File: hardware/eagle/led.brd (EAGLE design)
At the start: 160 x 100 mm, 15 parts, among them IC1 MCP1406SOIC8, IC10 MCP1406SOIC8, IC11 MCP1406SOIC8, IC12 MCP1406SOIC8, IC13 MCP2551SOIC8, IC2 MCP1406SOIC8, IC3 MCP1406SOIC8, IC4 MCP1406SOIC8, IC5 MCP1406SOIC8, IC6 MCP1406SOIC8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

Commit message: neue boaerd version + datasheets added
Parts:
- removed JP1, JP2: (no value), pinhead:2X13
- added C2: (no value), rcl:E5-10,5
- added EXT1, EXT2: (no value), pinhead:2X13
- added IC14: 7805T, linear:TO220H
- added U$1, U$10, U$11, U$2, U$3, U$5, U$6, U$7, U$8, U$9: 2KLEMME, custom-parts:W237-102
- moved IC12 212.0 mm to (97.8, 74.9), flipped to the bottom
- moved IC10 189.5 mm to (82.5, 74.9), flipped to the bottom
- moved IC11 188.6 mm to (90.2, 74.9), flipped to the bottom
- moved IC13 167.5 mm to (50.8, 49.5), flipped to the bottom
- moved IC9 148.1 mm to (38.1, 74.9), flipped to the bottom
- moved IC6 144.5 mm to (90.2, 25.4), flipped to the bottom, turned to 180 degrees
- moved IC5 143.2 mm to (97.8, 25.4), flipped to the bottom, turned to 180 degrees
- moved IC4 142.0 mm to (105.4, 25.4), flipped to the bottom, turned to 180 degrees
- moved IC7 140.2 mm to (45.7, 74.9), flipped to the bottom
- moved IC8 139.3 mm to (53.3, 74.9), flipped to the bottom
- moved IC3 85.8 mm to (54.6, 25.4), flipped to the bottom, turned to 180 degrees
- moved IC2 84.6 mm to (62.2, 25.4), flipped to the bottom, turned to 180 degrees
- moved IC1 78.0 mm to (69.8, 25.4), flipped to the bottom, turned to 180 degrees
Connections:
- new net B1: EXT1.17, IC1.2
- new net B2: EXT1.26, IC4.2
- new net B3: EXT1.16, IC7.2
- new net B4: EXT2.10, IC10.2
- new net CANH: IC13.7, U$3.1
- new net CANL: IC13.6, U$3.2
- new net CANRX: EXT1.1, IC13.4
- new net CANTX: EXT1.3, IC13.1
- new net G1: EXT1.15, IC2.2
- new net G2: EXT1.22, IC5.2
- new net G3: EXT2.7, IC8.2
- new net G4: EXT2.8, IC11.2
- new net N$10: IC8.6, IC8.7, U$8.2
- new net N$11: IC7.6, IC7.7, U$7.1
- new net N$12: IC12.6, IC12.7, U$9.1
- new net N$13: IC11.6, IC11.7, U$9.2
- new net N$14: IC10.6, IC10.7, U$2.1
- new net N$2: C2.-, IC14.2, U$1.2
- new net N$3: IC3.6, IC3.7, U$5.1
- new net N$4: IC2.6, IC2.7, U$5.2
- new net N$5: IC1.6, IC1.7, U$6.1
- new net N$6: IC6.6, IC6.7, U$10.1
- new net N$7: IC5.6, IC5.7, U$10.2
- new net N$8: IC4.6, IC4.7, U$11.1
- new net N$9: IC9.6, IC9.7, U$8.1
- new net R1: EXT1.13, IC3.2
- new net R2: EXT1.21, IC6.2
- new net R3: EXT1.14, IC9.2
- new net R4: EXT2.4, IC12.2
- new net VCC: EXT2.26, IC13.3, IC14.3
- net +12V: now also C2.+, IC14.1, U$1.1, U$2.2
- net GND: now also EXT2.25, IC13.2, U$11.2, U$6.2, U$7.2
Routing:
- net R3: track 0.00 -> 45.8 mm
- net B3: track 0.00 -> 41.5 mm
- net B2: track 0.00 -> 33.5 mm
- net G2: track 0.00 -> 29.5 mm
- net R4: track 0.00 -> 28.7 mm
- net G4: track 0.00 -> 26.9 mm
- net G3: track 0.00 -> 26.5 mm
- net B4: track 0.00 -> 22.6 mm
- net R2: track 0.00 -> 21.6 mm
- net R1: track 0.00 -> 18.5 mm
- net G1: track 0.00 -> 14.9 mm
- net B1: track 0.00 -> 12.8 mm
- net CANRX: track 0.00 -> 11.3 mm
- net CANTX: track 0.00 -> 7.75 mm

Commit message: hardware changed
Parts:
- moved U$3 96.0 mm to (39.4, 3.81), turned to 0 degrees
- moved IC9 24.1 mm to (62.2, 74.9)
- moved IC13 16.3 mm to (40.6, 36.8), turned to 270 degrees
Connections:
- net +12V: no longer U$2.2
- net B3: now also EXT1.14; no longer EXT1.16
- net G3: now also EXT1.16; no longer EXT2.7
- net GND: now also U$2.2
- net R3: now also EXT2.7; no longer EXT1.14
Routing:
- net +12V: track 0.00 -> 119.6 mm
- net CANH: track 0.00 -> 41.1 mm
- net CANL: track 0.00 -> 34.9 mm
- net R3: track 45.8 -> 21.8 mm
- net N$8: track 0.00 -> 20.7 mm
- net N$11: track 0.00 -> 19.2 mm
- net CANRX: track 11.3 -> 0.00 mm
- net CANTX: track 7.75 -> 17.3 mm
- net B3: track 41.5 -> 34.4 mm
- net G3: track 26.5 -> 32.0 mm
- added copper zone on layer 16, net GND

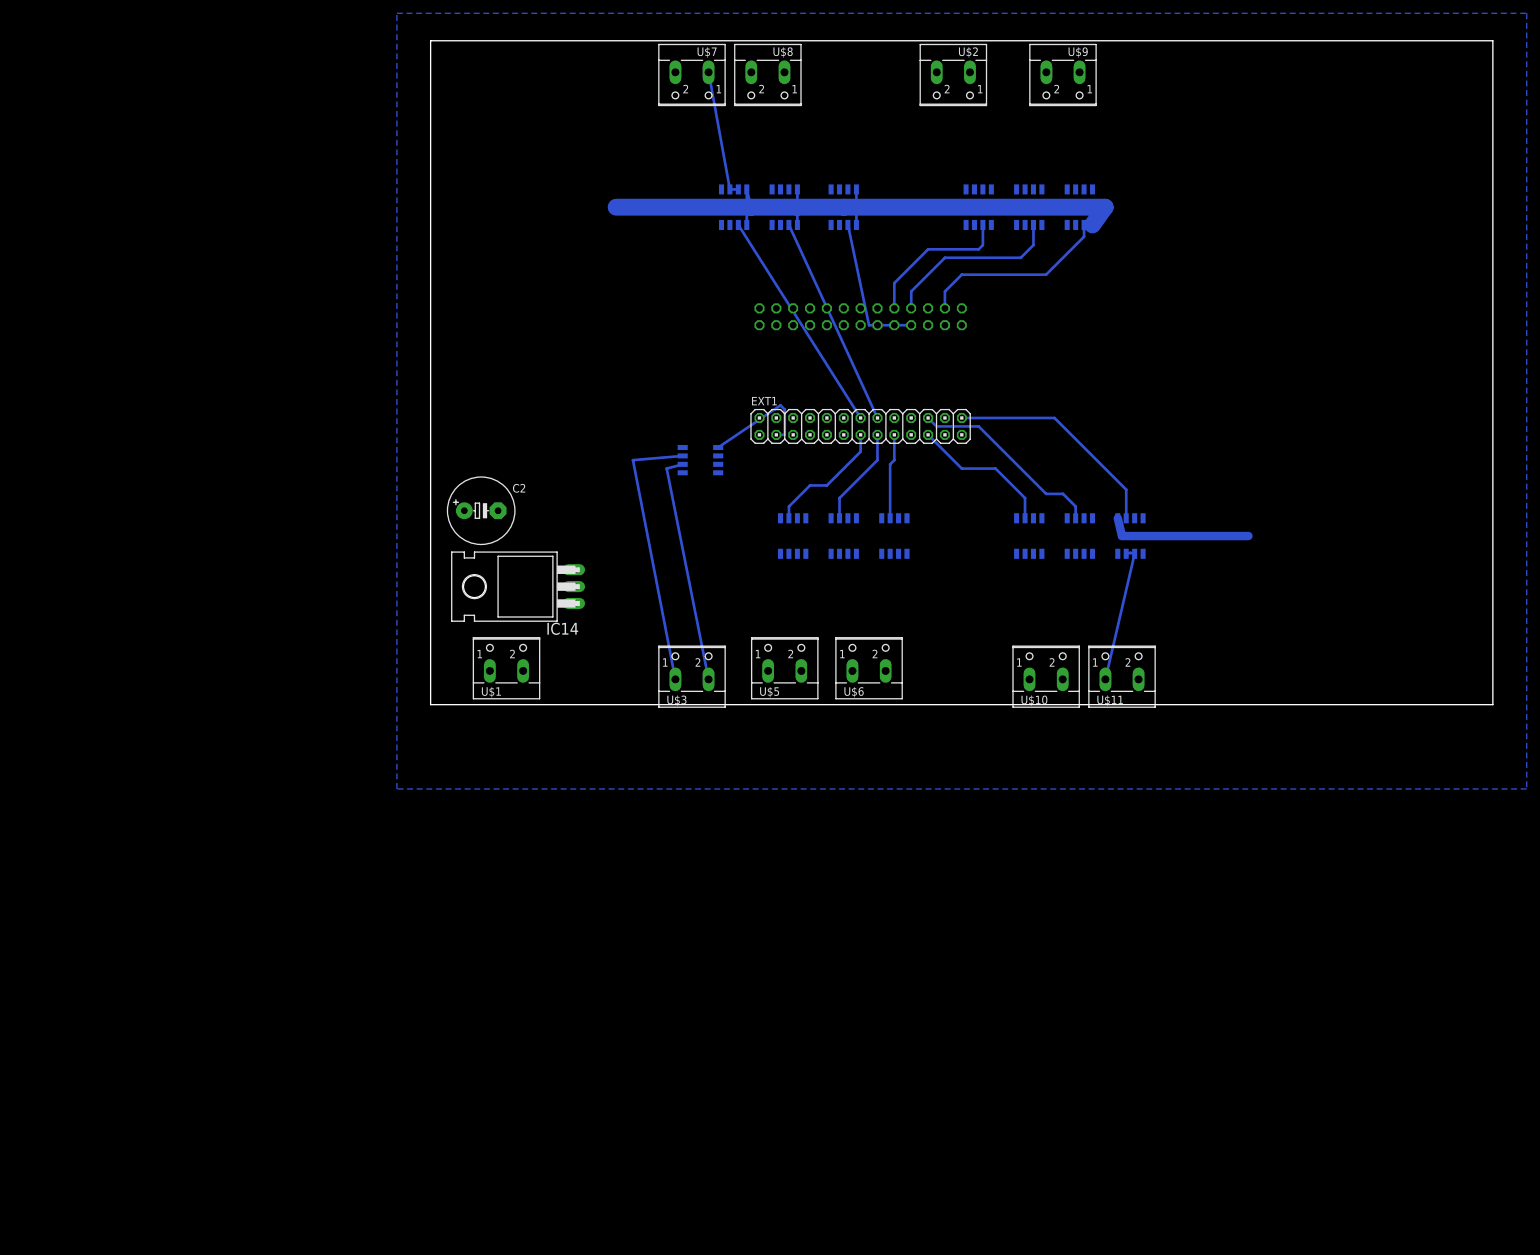
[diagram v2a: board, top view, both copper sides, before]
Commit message: neues board nicht fertig geroutet wegen kreuzungen
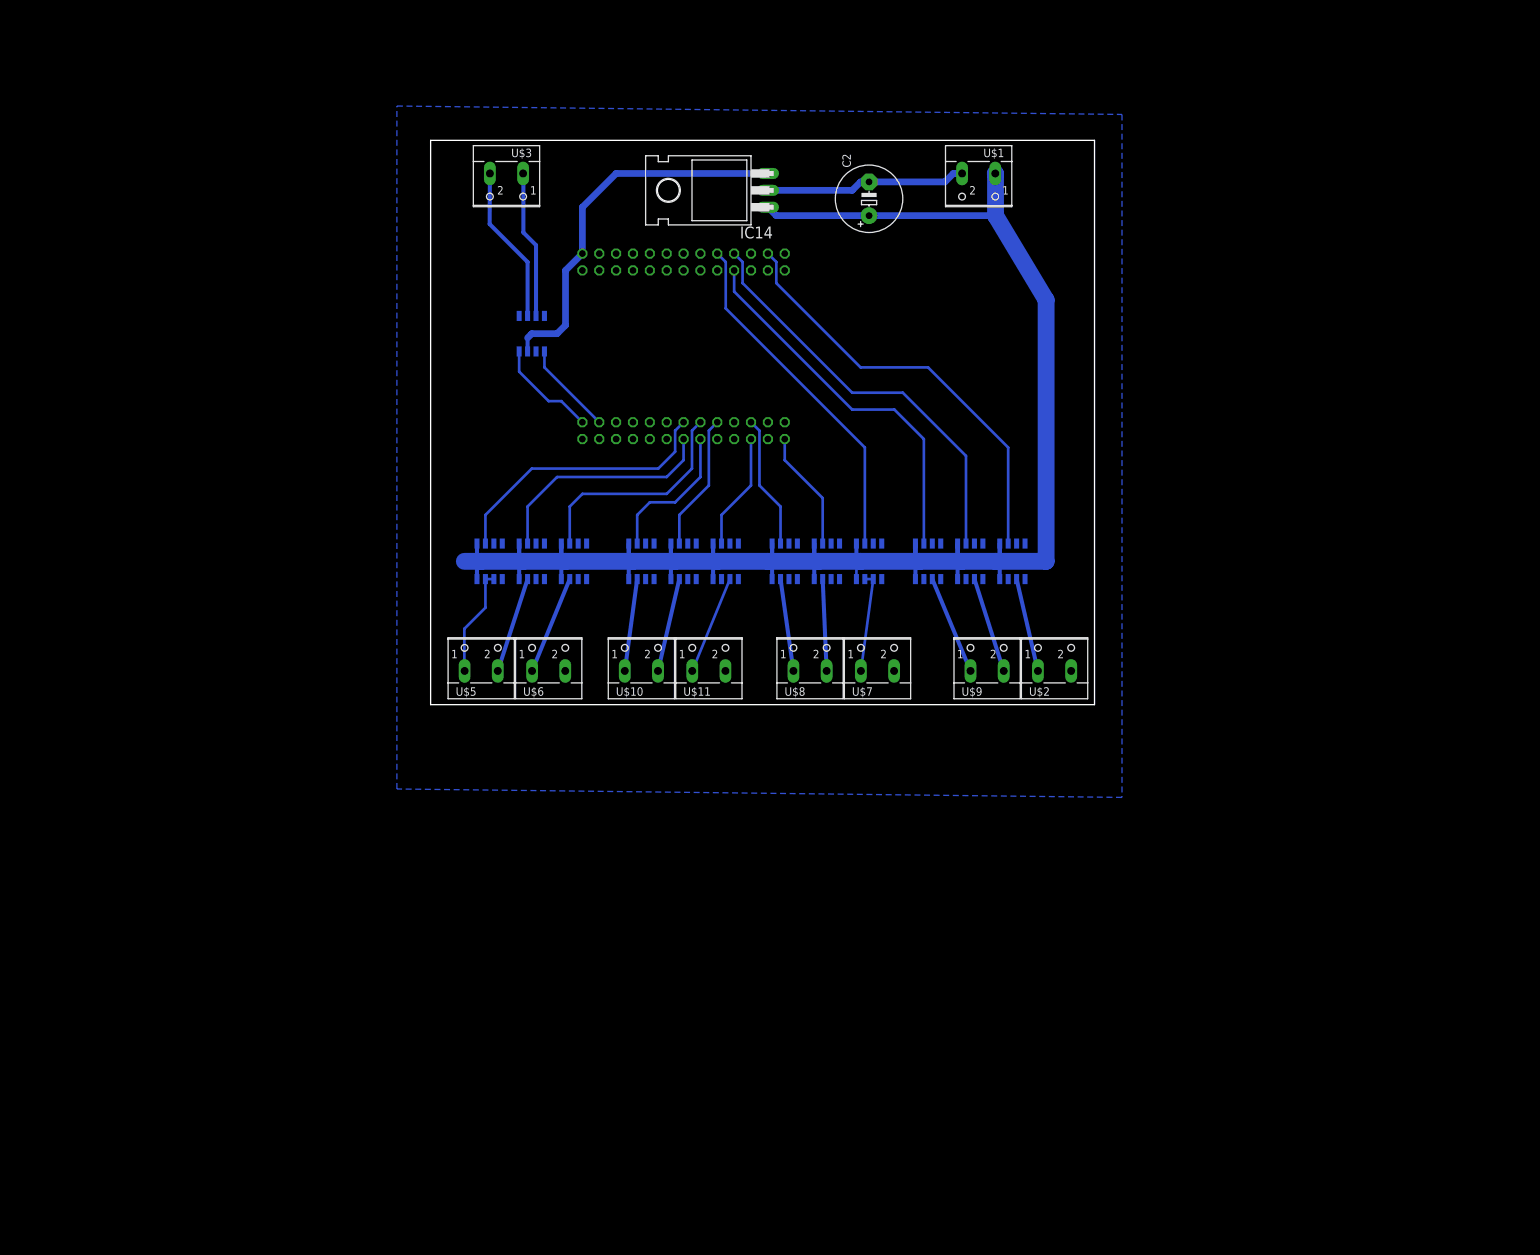
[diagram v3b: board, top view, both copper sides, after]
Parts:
- moved U$1 103.3 mm to (82.5, 80.0), turned to 180 degrees
- moved U$7 94.4 mm to (67.3, 5.08), turned to 0 degrees
- moved U$2 91.4 mm to (94.0, 5.08), turned to 0 degrees
- moved U$9 90.9 mm to (83.8, 5.08), turned to 0 degrees
- moved U$8 90.4 mm to (57.1, 5.08), turned to 0 degrees
- moved U$3 81.2 mm to (11.4, 80.0), turned to 180 degrees
- moved C2 75.0 mm to (66.0, 76.2), turned to 90 degrees
- moved IC14 66.5 mm to (40.6, 77.5)
- moved U$11 62.2 mm to (41.9, 5.08)
- moved IC4 61.1 mm to (44.5, 21.6)
- moved U$10 61.0 mm to (31.8, 5.08)
- moved IC5 59.8 mm to (38.1, 21.6)
- moved IC6 58.5 mm to (31.8, 21.6)
- moved IC12 58.0 mm to (74.9, 21.6), turned to 180 degrees
- moved IC7 57.1 mm to (66.0, 21.6), turned to 180 degrees
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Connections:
- net B1: now also EXT1.15; no longer EXT1.17
- net B2: now also EXT1.22; no longer EXT1.26
- net B3: now also EXT2.10; no longer EXT1.14
- net B4: now also EXT2.4; no longer EXT2.10
- net G1: now also EXT1.14; no longer EXT1.15
- net G2: now also EXT1.17; no longer EXT1.22
- net G3: now also EXT1.26; no longer EXT1.16
- net R2: now also EXT1.16; no longer EXT1.21
- net R3: now also EXT1.21; no longer EXT2.7
- net R4: now also EXT2.7; no longer EXT2.4
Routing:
- net +12V: track 119.6 -> 286.9 mm
- net VCC: track 0.00 -> 57.4 mm
- net B4: track 22.6 -> 64.6 mm
- net G4: track 26.9 -> 62.6 mm
- net N$2: track 0.00 -> 30.3 mm
- net R4: track 28.7 -> 56.7 mm
- net R1: track 18.5 -> 41.8 mm
- net B1: track 12.8 -> 33.9 mm
- net G1: track 14.9 -> 35.1 mm
- net CANH: track 41.1 -> 22.3 mm
- net B3: track 34.4 -> 52.9 mm
- net N$3: track 0.00 -> 16.4 mm
- net B2: track 33.5 -> 17.6 mm
- net CANRX: track 0.00 -> 15.7 mm
- net N$12: track 0.00 -> 15.0 mm
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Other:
- board size 160 x 100 mm -> 100 x 85 mm

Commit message: nur noch 2 drahtbrücken im layout: TODO buchsen nach löschen ausrichten
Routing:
- net N$3: track 16.4 -> 1.27 mm
- net N$12: track 15.0 -> 0.00 mm
- net N$8: track 15.0 -> 0.00 mm
- net N$5: track 15.0 -> 0.00 mm
- net N$4: track 14.5 -> 0.00 mm
- net N$13: track 14.5 -> 0.00 mm
- net N$7: track 14.2 -> 0.00 mm
- net N$14: track 14.2 -> 0.00 mm
- net N$9: track 14.0 -> 0.00 mm
- net N$6: track 14.0 -> 0.00 mm
- net N$11: track 15.2 -> 1.27 mm
- net N$10: track 13.8 -> 0.00 mm
- net B3: track 52.9 -> 54.7 mm
- net R1: track 41.8 -> 40.7 mm
- net G2: track 20.6 -> 21.7 mm

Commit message: einige datein mal mit commitet da die sonst immer vergessen wurden
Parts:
- removed IC14: 7805T, linear:TO220H
- added C1, C3: 10nF, rcl:C025-025X050
- added D1, D2, D3, D9: 1N4001, diode:MELF-MLL41
- added F2: FUSESH35, fuse:SH25
- added IC15: 7805TV, linear:TO220V
- added JP3: LEDS, pinhead:1X04
- added R1, R2, R3: 280R, rcl:0204/7
- C2: value (none) -> 1000µF; device rcl:E5-10,5 -> rcl:E5-8,5
- U$3: value 2KLEMME -> 3KLEMME; device custom-parts:W237-102 -> custom-parts:W237-103
- moved C2 29.8 mm to (86.5, 54.5), turned to 180 degrees
- moved U$1 18.8 mm to (63.8, 80.5)
- moved U$5 6.46 mm to (14.1, 4.85)
- moved U$6 6.46 mm to (24.2, 4.85)
- moved EXT1 4.90 mm to (43.0, 41.3)
- moved EXT2 4.90 mm to (43.0, 66.7)
- moved U$2 3.71 mm to (90.3, 4.85)
- moved U$9 3.71 mm to (80.1, 4.85)
- moved U$11 2.66 mm to (44.6, 4.85)
- moved U$10 2.66 mm to (34.4, 4.85)
- moved U$8 2.66 mm to (59.8, 4.85)
- moved U$7 2.66 mm to (70.0, 4.85)
- moved U$3 2.01 mm to (13.4, 80.5)
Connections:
- removed net VCC: EXT2.26, IC13.3, IC14.3
- new net +5V: C1.1, D9.A, EXT2.26, IC13.3, IC15.3
- new net LED1: EXT2.20, R1.2
- new net LED2: EXT2.21, R2.2
- new net LED3: EXT2.22, R3.2
- new net N$1: C3.1, D1.C, D9.C, IC15.1
- new net N$32: JP3.1, R1.1
- new net N$36: JP3.2, R2.1
- new net N$37: JP3.3, R3.1
- net +12V: now also D1.A, D2.C, D3.C, U$1.2; no longer IC14.1, U$1.1
- net GND: now also C1.2, C2.-, C3.2, D2.A, D3.A, F2.2, IC13.8, IC15.2, IC8.4, JP3.4, U$3.3
- net N$2: now also F2.1, U$1.1; no longer C2.-, IC14.2, U$1.2
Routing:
- net GND: track 0.00 -> 94.4 mm, vias 0 -> 27
- net +5V: track 0.00 -> 57.9 mm
- net VCC: track 57.4 -> 0.00 mm
- net N$37: track 0.00 -> 27.4 mm
- net N$1: track 0.00 -> 27.4 mm
- net N$2: track 30.3 -> 6.07 mm
- net N$36: track 0.00 -> 20.8 mm
- net N$8: track 0.00 -> 17.0 mm
- net N$12: track 0.00 -> 16.3 mm
- net N$9: track 0.00 -> 16.3 mm
- net N$32: track 0.00 -> 16.2 mm
- net N$7: track 0.00 -> 16.2 mm
- net N$10: track 0.00 -> 16.0 mm
- net N$4: track 0.00 -> 16.0 mm
- net N$5: track 0.00 -> 15.7 mm
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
